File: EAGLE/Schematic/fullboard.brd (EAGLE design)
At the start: 100.9 x 77.1 mm, 87 parts, among them CN1 B4B-ZR, CN2 B4B-ZR, CN3 B4B-ZR, CN4 S4B-ZR, CN5 S4B-ZR, CN6 S4B-ZR, CN7 S4B-ZR, CN8 S4B-ZR, CN9 S4B-ZR, IC1 IFX007T, IC2 IFX007T, IC3 IFX007T, IC4 IFX007T, J1 10118193-0001LF, Q1 8MHz ±10ppm Crystal 18pF 80 O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, SW1 TR1-SPST, U1 ATXMEGA128A3U-AU, U2 FT232RL-REEL

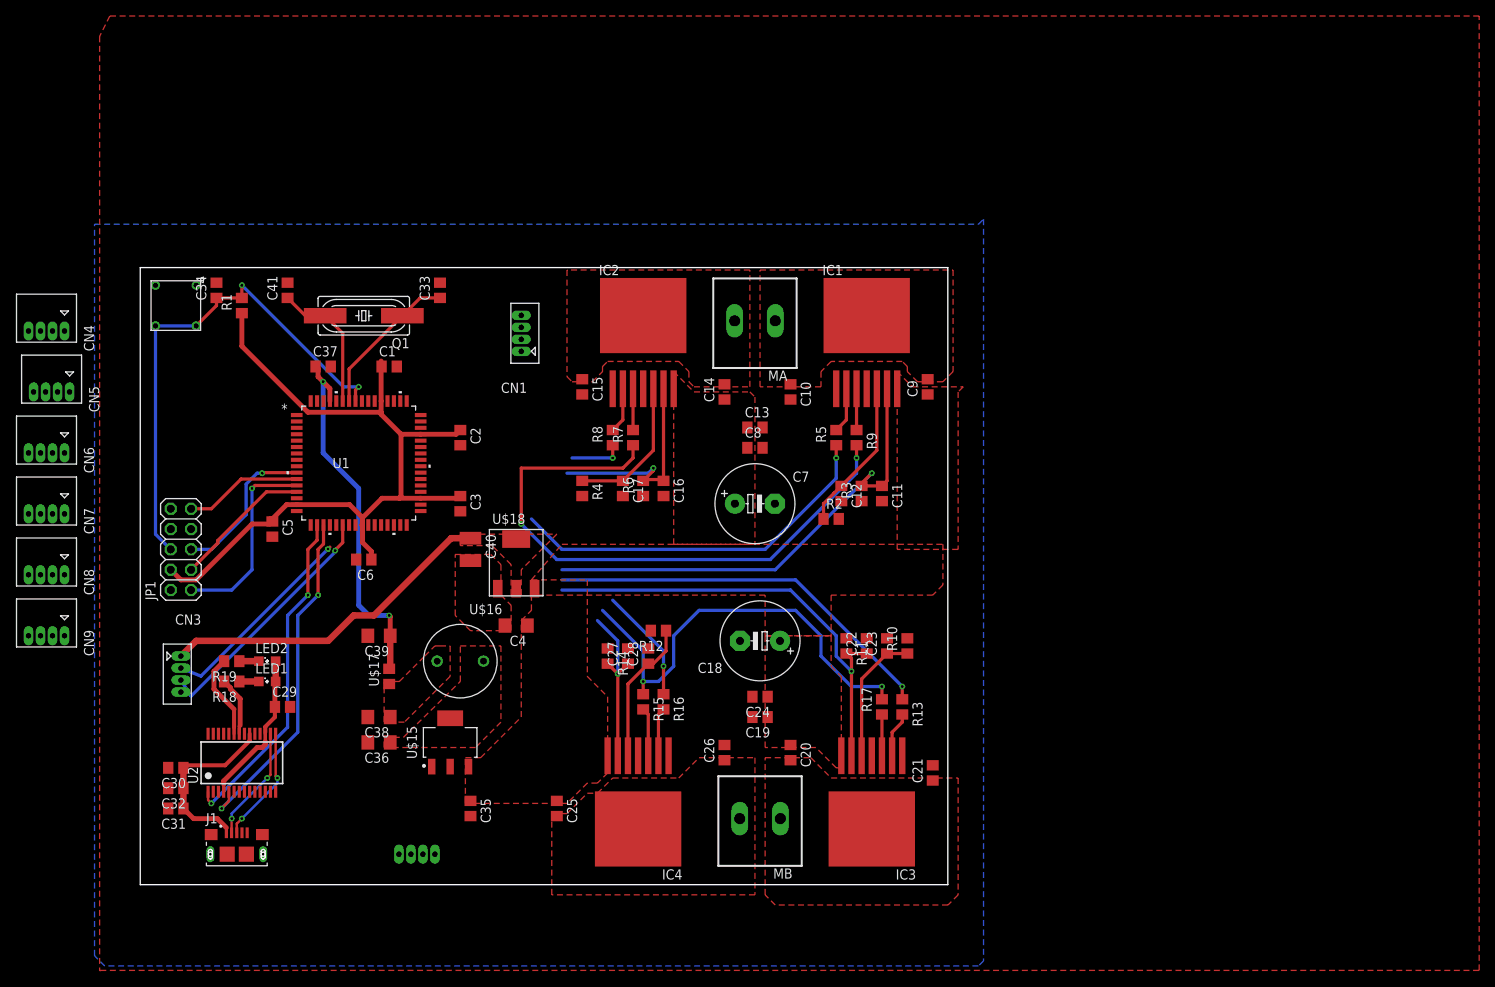
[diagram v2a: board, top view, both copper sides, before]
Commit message: V0.3
Don't you dare put a fucking fuse holder on the board.

Added:
* Routing all the remaining signals
* Vias for breakout of leftover pins
* Now with 200% more suffering

Still to do:
* Things
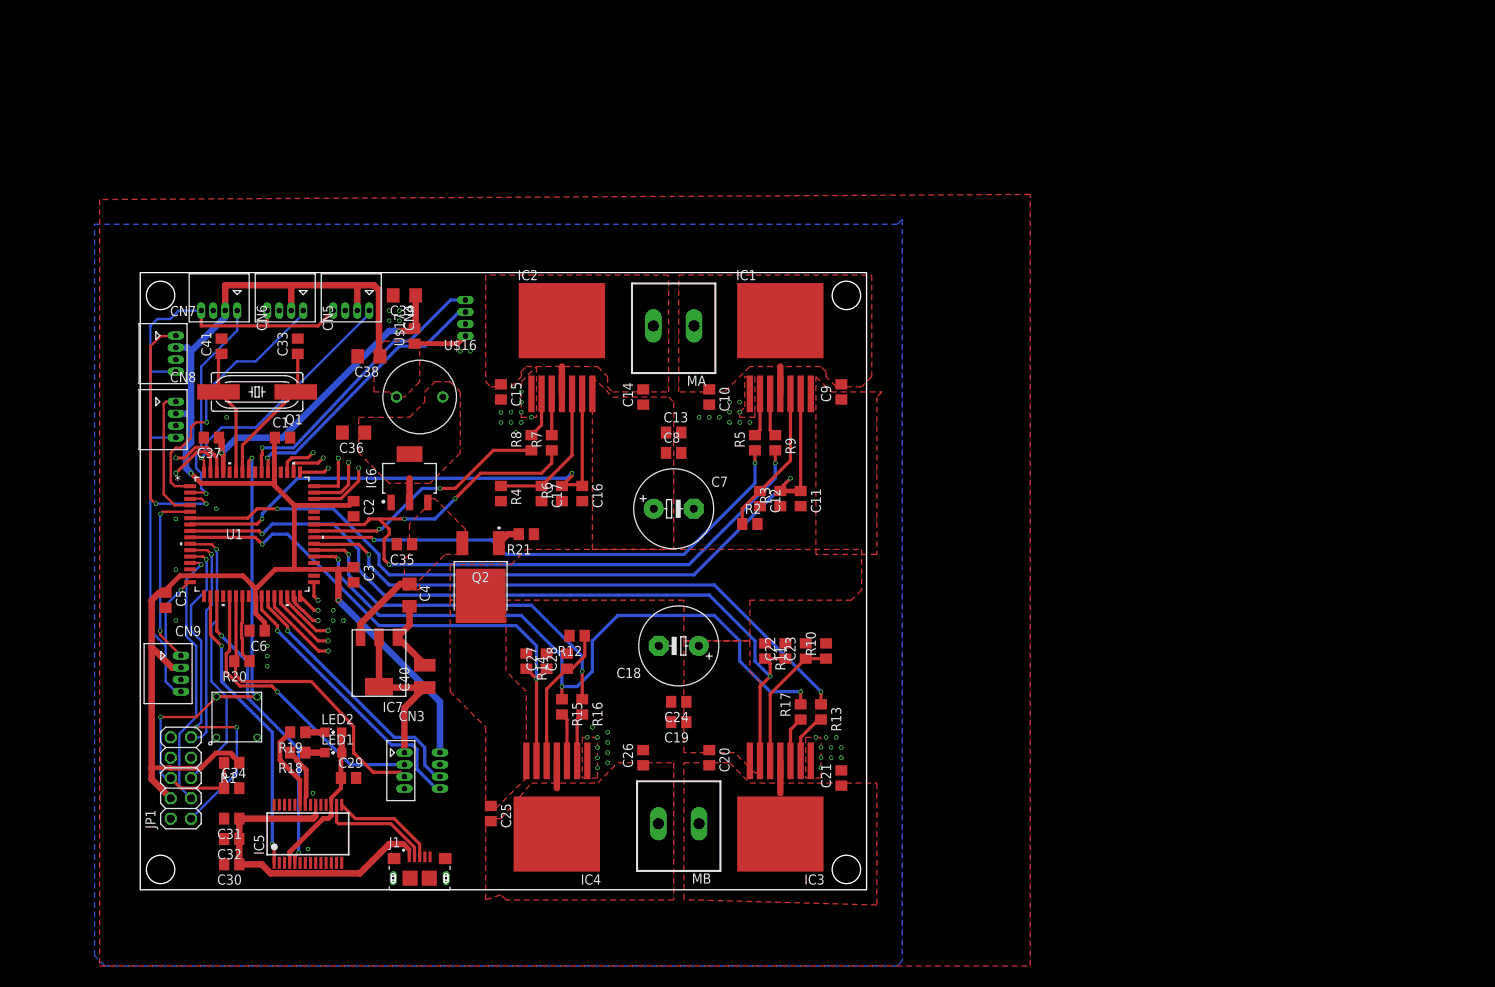
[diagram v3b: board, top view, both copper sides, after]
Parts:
- removed U$15: LDL1117S33R, SumBot:SOT230P700X190-4N
- removed U$18: AZ1117IH, SumBot:SOT223
- removed U2: FT232RL-REEL, FT232RL-REEL:SOP65P780X200-28N
- added IC5: FT232RL-REEL, FT232RL-REEL:SOP65P780X200-28N
- added IC6: LDL1117S33R, SumBot:SOT230P700X190-4N
- added IC7: AZ1117IH, SumBot:SOT223
- added Q2: AOD4189, AOD4189:AOD480
- added R20: 47Ω, rcl:R0805
- added R21: 10kΩ, rcl:R0805
- moved C34 62.3 mm to (11.4, 12.7), turned to 0 degrees
- moved R1 57.2 mm to (11.4, 15.9), turned to 180 degrees
- moved SW1 52.0 mm to (12.1, 21.6), turned to 270 degrees
- moved C38 45.1 mm to (28.6, 66.7)
- moved C39 42.7 mm to (33.0, 74.3)
- moved U$17 42.7 mm to (34.3, 69.2)
- moved C36 38.9 mm to (26.7, 57.1)
- moved CN4 38.2 mm to (24.1, 72.4)
- moved C35 34.0 mm to (33.0, 43.2), turned to 180 degrees
- moved U$16 33.4 mm to (34.9, 61.6)
- moved CN5 30.9 mm to (15.9, 72.4)
- moved CN3 30.4 mm to (33.0, 17.1)
- moved JP1 28.6 mm to (5.08, 14.0)
- moved CN6 28.0 mm to (7.62, 72.4)
- moved CN7 25.6 mm to (4.45, 64.8), turned to 90 degrees
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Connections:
- removed net CS_A: C11.1, C16.1, IC1.6, IC2.6, R3.2, R6.2
- removed net CS_B: C22.1, C27.1, IC3.6, IC4.6, R11.2, R14.2
- new net N$14: R20.1, U1.23
- new net N$36: C35.1, C4.1, IC6.3, IC7.3, Q2.3
- new net N$37: Q2.1, R21.2
- new net N$38: U1.46
- new net N$39: U1.47
- new net N$40: U1.48
- new net N$41: U1.49
- new net N$42: U1.50
- new net N$43: U1.51
- new net N$44: U1.33
- new net N$45: U1.32
- new net N$46: U1.31
- new net N$47: U1.30
- new net N$48: U1.29
- new net N$49: U1.28
- new net N$50: U1.62
- new net N$51: U1.63
- net +12V: now also Q2.2; no longer C35.1, C4.1, U$15.3, U$18.3
- net +5V: now also IC7.2, IC7.4; no longer U$18.2, U$18.4
- net CSB_A: now also C16.1, IC2.6, R6.2
- net CSB_B: now also C27.1, IC4.6, R14.2
- net CSF_A: now also C11.1, IC1.6, R3.2
- net CSF_B: now also C22.1, IC3.6, R11.2
- net GND: now also IC5.18, IC5.21, IC5.25, IC5.26, IC5.7, IC6.1, R21.1; no longer U$15.1, U2.18, U2.21, U2.25, U2.26, U2.7
- net N$1: now also IC7.1; no longer U$18.1
- net N$18: now also IC5.16; no longer U2.16
- net N$19: now also IC5.15; no longer U2.15
- net N$21: now also IC5.23; no longer U2.23
- net N$22: now also IC5.22; no longer U2.22
- net N$24: now also IC5.27; no longer U2.27
- net N$25: now also IC5.9; no longer U2.9
- net N$26: now also IC5.11; no longer U2.11
- net N$27: now also IC5.28; no longer U2.28
- net N$28: now also IC5.2; no longer U2.2
- net N$29: now also IC5.3; no longer U2.3
- net N$30: now also IC5.13; no longer U2.13
- net N$31: now also IC5.14; no longer U2.14
- net N$32: now also IC5.12; no longer U2.12
- net N$33: now also IC5.6; no longer U2.6
- net N$34: now also IC5.10; no longer U2.10
- net N$35: now also IC5.19; no longer U2.19
- net N$8: now also IC6.2, IC6.4; no longer U$15.2, U$15.4
- net RX_FT232: now also IC5.1; no longer U2.1
- net TX/RX_MSE: now also R20.2; no longer U1.23
- net TX_FT232: now also IC5.5; no longer U2.5
- net USB_PWR: now also IC5.20; no longer U2.20
- net VCCIO: now also IC5.17, IC5.4; no longer U2.17, U2.4
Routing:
- net +3V3: track 99.9 -> 212.3 mm, vias 0 -> 2
- net CSF_A: track 0.00 -> 101.5 mm, vias 0 -> 2
- net CSF_B: track 0.00 -> 100.2 mm, vias 0 -> 2
- net EDGE_CTRL: track 0.00 -> 91.6 mm, vias 0 -> 1
- net CS_A: track 88.8 -> 0.00 mm, vias 2 -> 0
- net CS_B: track 79.0 -> 0.00 mm, vias 2 -> 0
- net CSB_B: track 0.00 -> 67.9 mm, vias 0 -> 2
- net CSB_A: track 0.00 -> 67.1 mm, vias 0 -> 2
- net EB_A: track 0.00 -> 36.4 mm, vias 0 -> 1
- net EB_B: track 0.00 -> 35.1 mm, vias 0 -> 1
- net EA_A: track 0.00 -> 34.2 mm, vias 0 -> 1
- net EDGE_B: track 0.00 -> 33.5 mm, vias 0 -> 1
- net EA_B: track 0.00 -> 33.2 mm, vias 0 -> 1
- net EDGE_D: track 0.00 -> 32.3 mm, vias 0 -> 2
- net EDGE_A: track 0.00 -> 31.5 mm, vias 0 -> 1
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- added copper zone on layer 1, net N$36
- removed copper zone on layer 1, net +5V
- removed copper zone on layer 1, net N$1
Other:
- board size 100.9 x 77.1 mm -> 90.8 x 77.1 mm

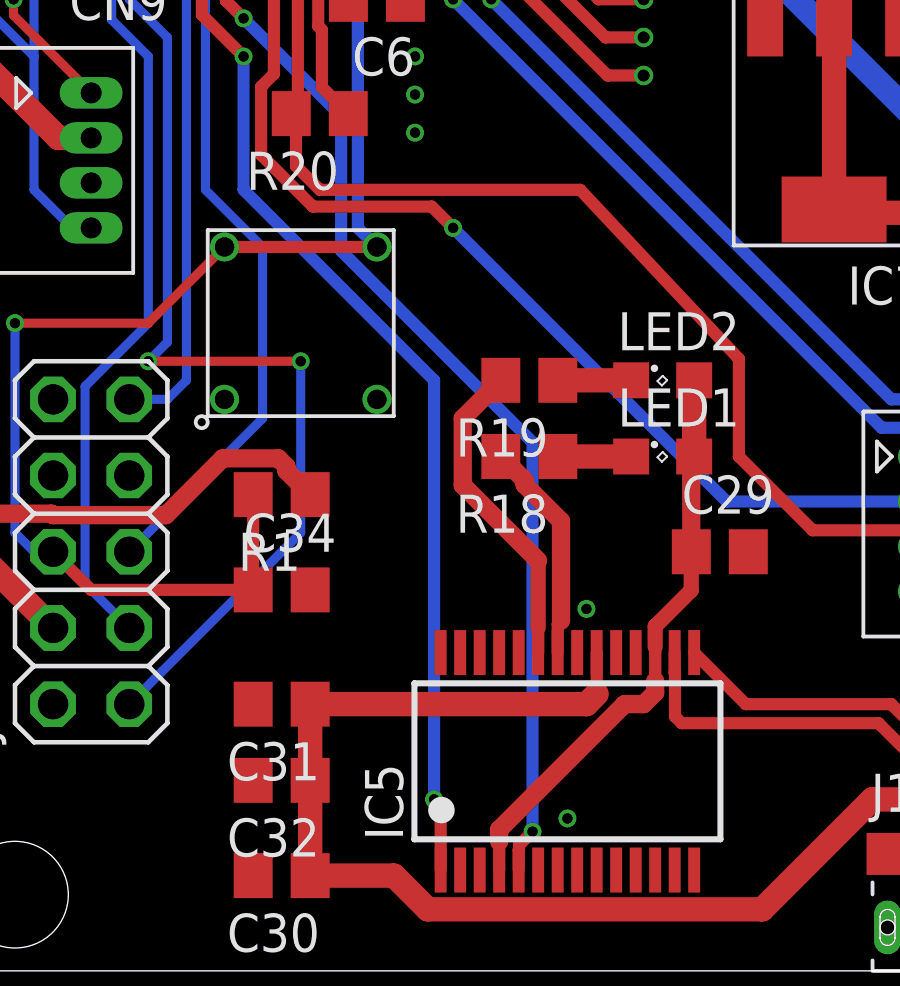
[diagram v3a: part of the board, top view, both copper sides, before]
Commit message: V0.4
Added vias as test points for the two USART channels
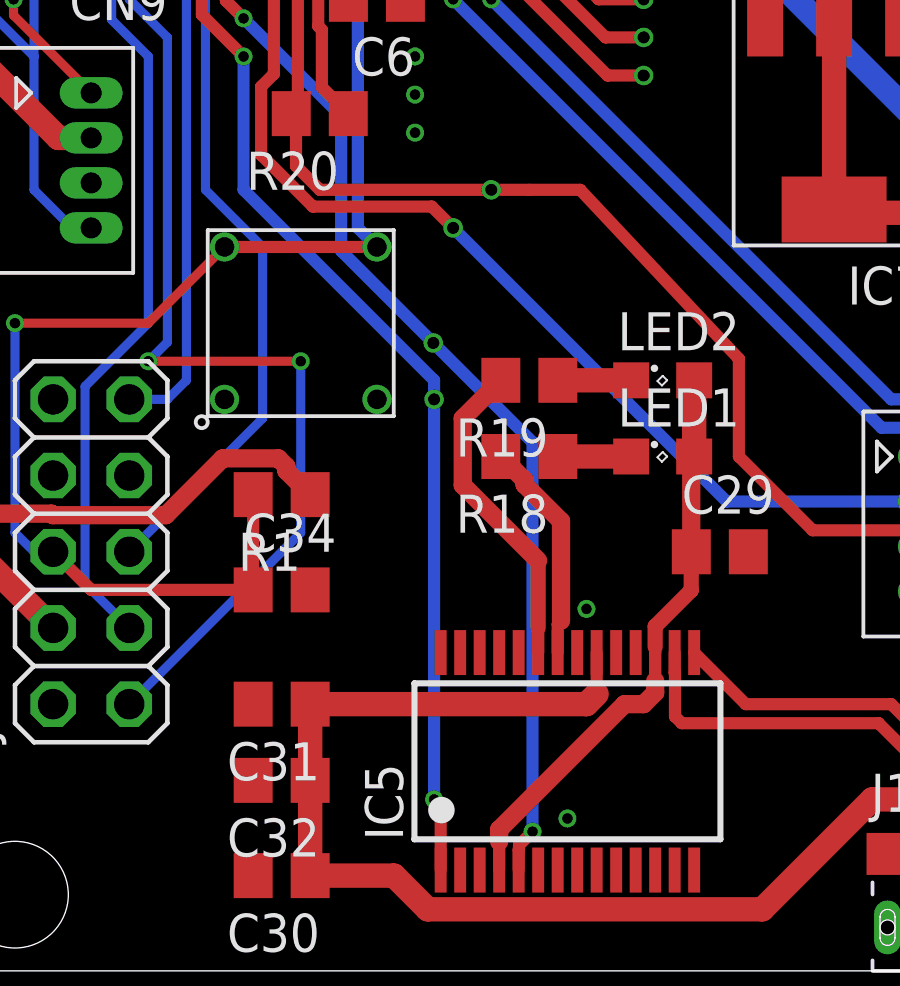
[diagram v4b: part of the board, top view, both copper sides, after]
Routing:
- net XCK_MSE: vias 1 -> 2
- net TX_FT232: vias 2 -> 3
- net TX/RX_MSE: vias 0 -> 1
- net RX_FT232: vias 2 -> 3
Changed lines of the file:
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@@
 <wire x1="10.16" y1="30.48" x2="8.77" y2="31.87" width="0.4064" layer="1"/>
 <wire x1="8.77" y1="31.87" x2="8.77" y2="36.703" width="0.4064" layer="1"/>
+<wire x1="16.51" y1="19.05" x2="16.51" y2="19.685" width="0.4064" layer="16"/>
 <wire x1="16.51" y1="19.685" x2="10.16" y2="26.035" width="0.4064" layer="16"/>
 <wire x1="10.16" y1="30.48" x2="10.16" y2="26.035" width="0.4064" layer="16"/>
-<wire x1="16.51" y1="19.685" x2="16.51" y2="5.715" width="0.4064" layer="16"/>
+<wire x1="16.51" y1="19.05" x2="16.51" y2="5.715" width="0.4064" layer="16"/>
+<via x="16.51" y="19.05" extent="1-16" drill="0.4"/>
 </signal>
 <signal name="TX_FT232">
@@
 <wire x1="13.4112" y1="28.4988" x2="13.4112" y2="24.002075" width="0.4064" layer="16"/>
 <wire x1="19.7920375" y1="17.6212375" x2="19.7920375" y2="4.6406" width="0.4064" layer="16"/>
-<wire x1="13.4112" y1="24.002075" x2="19.7920375" y2="17.6212375" width="0.4064" layer="16"/>
+<wire x1="13.4112" y1="24.002075" x2="16.4841375" y2="20.9291375" width="0.4064" layer="16"/>
+<wire x1="16.4841375" y1="20.9291375" x2="19.7920375" y2="17.6212375" width="0.4064" layer="16"/>
+<via x="16.4841375" y="20.9291375" extent="1-16" drill="0.4"/>
 </signal>
 <signal name="XCK_MSE">
@@
 <wire x1="12.46853125" y1="25.4762" x2="10.7444" y2="27.20033125" width="0.4064" layer="1"/>
 <wire x1="10.7444" y1="27.20033125" x2="10.7444" y2="29.47229375" width="0.4064" layer="1"/>
+<via x="17.145" y="24.765" extent="1-16" drill="0.4"/>
 </signal>
 <signal name="TX/RX_MSE">
@@
 <wire x1="11.9075" y1="28.7325" x2="11.75" y2="28.575" width="0.4064" layer="1"/>
 <wire x1="33.02" y1="14.145" x2="32.4796" y2="14.6854" width="0.4064" layer="1"/>
-<wire x1="21.38145625" y1="26.035" x2="12.7" y2="26.035" width="0.4064" layer="1"/>
+<wire x1="21.38145625" y1="26.035" x2="19.685" y2="26.035" width="0.4064" layer="1"/>
+<wire x1="19.685" y1="26.035" x2="18.415" y2="26.035" width="0.4064" layer="1"/>
+<wire x1="18.415" y1="26.035" x2="12.7" y2="26.035" width="0.4064" layer="1"/>
 <wire x1="32.4796" y1="14.6854" x2="29.1296" y2="14.6854" width="0.4064" layer="1"/>
 <wire x1="29.1296" y1="14.6854" x2="26.67" y2="17.145" width="0.4064" layer="1"/>
@@
 <wire x1="12.7" y1="26.035" x2="11.9075" y2="26.8275" width="0.4064" layer="1"/>
 <wire x1="11.9075" y1="26.8275" x2="11.9075" y2="28.7325" width="0.4064" layer="1"/>
+<via x="18.415" y="26.035" extent="1-16" drill="0.4"/>
 </signal>
 <signal name="EB_A">

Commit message: v0.5
Changes/Status
* Silkscreen - done, do a final check after walking away for a bit
* Mounting - #4 screws - moved the ones I could the way I could
* AREF - should be ok, made vias for use of jumpering if needed.

Todo:
* Final check by Charlie
* ...
* profit
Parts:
- added BATT: (no value), ME507:2POL508
- moved C10 2.54 mm to (68.6, 61.6)
- moved IC3 1.91 mm to (78.1, 18.4)
- moved C20 1.27 mm to (69.8, 16.5)
- moved IC1 1.27 mm to (78.7, 59.7)
- moved R3 1.27 mm to (78.7, 48.9)
- moved C14 1.27 mm to (61.6, 61.6)
- moved C15 1.27 mm to (43.8, 62.2)
- moved C26 1.27 mm to (61.6, 16.5)
- moved R4 1.27 mm to (43.8, 49.5)
- moved R7 1.27 mm to (50.2, 55.9)
- moved R8 1.27 mm to (47.6, 55.9)
- moved C41 1.27 mm to (11.4, 67.9)
- moved C11 1.27 mm to (81.3, 48.9)
- moved C12 1.27 mm to (76.2, 48.9)
- moved C13 1.27 mm to (65.4, 57.1)
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- renumbered CN4 to E_A, CN5 to E_B, CN6 to E_C, CN7 to E_D, CN8 to E_E, CN9 to E_F, U$16 to L1, U$17 to L2
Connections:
- net +12V: now also BATT.2
- net GND: now also BATT.1
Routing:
- net EDGE_D: track 32.3 -> 26.0 mm
- net +3V3: track 212.3 -> 216.3 mm, vias 2 -> 3
- net N$16: track 6.40 -> 8.30 mm
- net EN_A: track 97.6 -> 95.8 mm
- net N$15: track 5.69 -> 7.22 mm
- net N$49: track 10.3 -> 11.9 mm
- net N$43: track 4.96 -> 6.39 mm
- net BCK_A: track 31.4 -> 30.1 mm
- net FWD_A: track 63.8 -> 62.5 mm
- net CSB_A: track 67.1 -> 65.8 mm
- net CSF_A: track 101.5 -> 100.2 mm
- net N$36: track 10.8 -> 9.85 mm
- net !RESET: track 64.1 -> 65.0 mm
- net N$48: track 8.79 -> 9.68 mm
- net N$10: track 17.2 -> 18.0 mm
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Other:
- board text added: "+"
- board text added: "-"
- board text added: "0"
- board text added: "2"
- board text added: "3"
- board text added: "7"
- board text added: "AVCC"
- board text added: "CLK"
- board text added: "FT232"
- board text added: "MSE"
- board text added: "PA0"
- board text added: "PA1"
- board text added: "PD"
- board text added: "PF"
- board text added: "RX"
- board text added: "TX"
- board text added: "TX/RX"
